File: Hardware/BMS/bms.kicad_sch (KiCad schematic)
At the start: 13 parts, among them J101 Conn_01x02, J102 Conn_02x05_Top_Bottom, J103 Conn_02x02_Counter_Clockwise, U101 74AHC1G08, U103 LTV-356T, U402 TSC2011IST

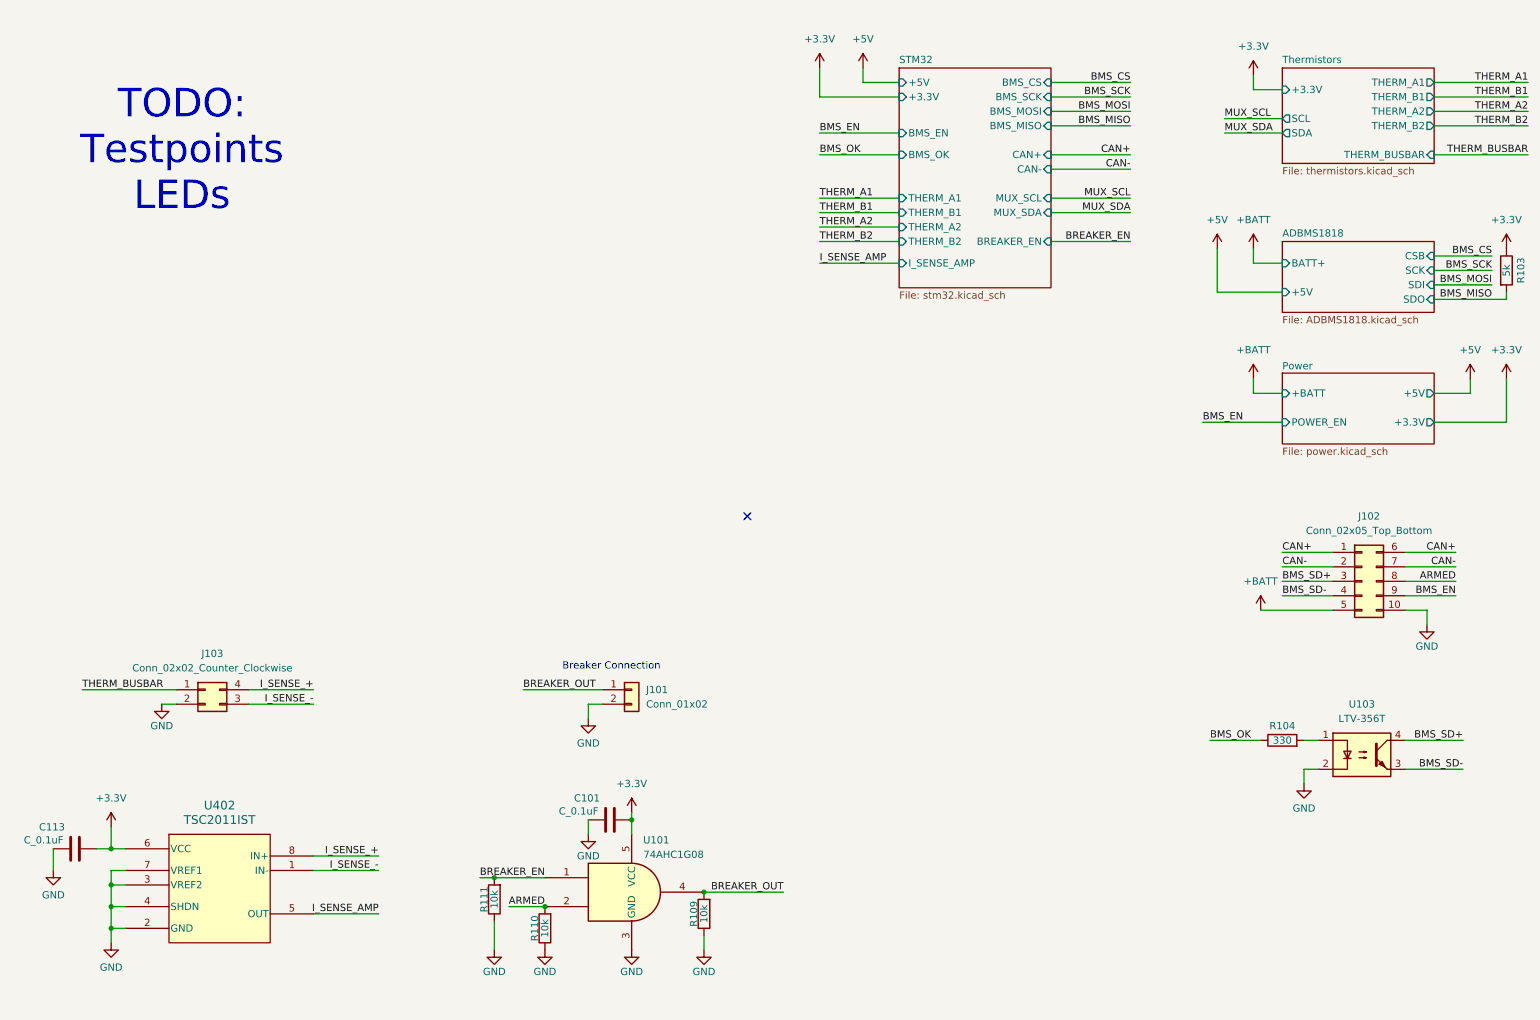
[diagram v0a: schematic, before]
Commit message: Add test points and LEDs
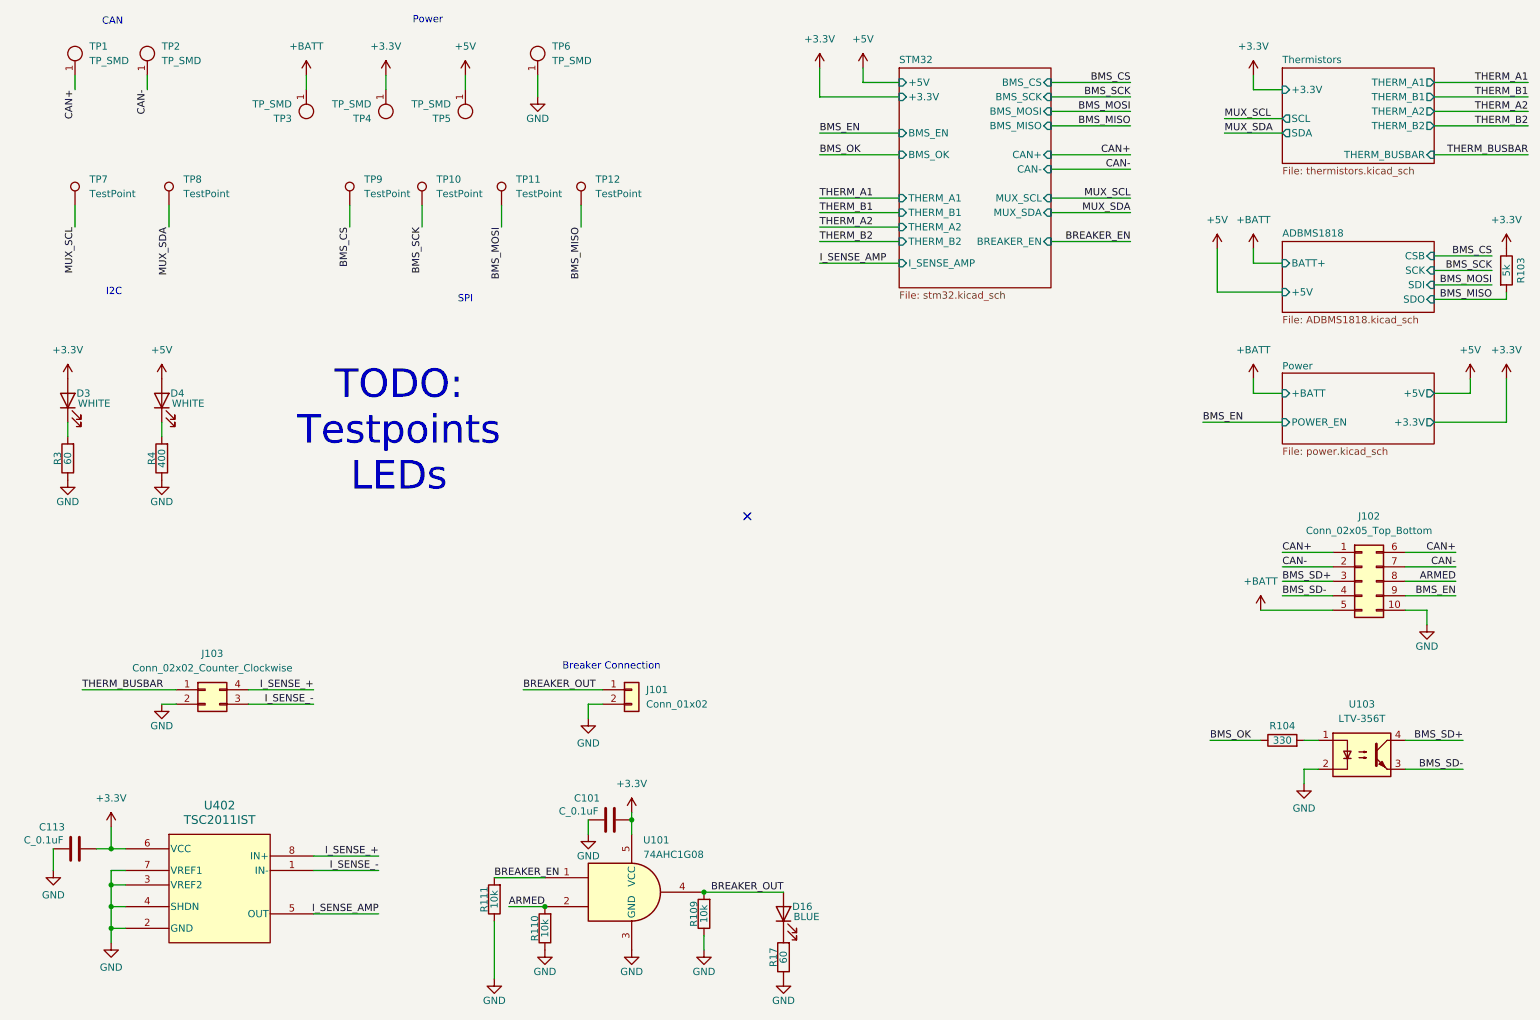
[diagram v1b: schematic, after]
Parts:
- added D16: BLUE, LED_SMD:LED_0805_2012Metric, symbol Device:LED
- added D3, D4: WHITE, LED_SMD:LED_0805_2012Metric, symbol Device:LED
- added R17, R3: 60, Resistor_SMD:R_0603_1608Metric, symbol Device:R
- added R4: 400, Resistor_SMD:R_0603_1608Metric, symbol Device:R
- added TP1, TP2, TP3, TP4, TP5, TP6: TP_SMD, TestPoint:TestPoint_Keystone_5019_Miniature, symbol formula:TP_SMD
- added TP10, TP11, TP12, TP7, TP8, TP9: TestPoint, TestPoint:TestPoint_Pad_1.0x1.0mm, symbol Connector:TestPoint
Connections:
- net +3.3V: now also D3.2 (A), TP4.1
- net +5V: now also D4.2 (A), TP5.1
- net +BATT: now also TP3.1
- net BMS_CS: now also TP9.1
- net BMS_MISO: now also TP12.1
- net BMS_MOSI: now also TP11.1
- net BMS_SCK: now also TP10.1
- net BREAKER_OUT: now also D16.2 (A)
- net CAN+: now also TP1.1
- net CAN-: now also TP2.1
- net GND: now also R17.1, R3.1, R4.1, TP6.1
- net MUX_SCL: now also TP7.1
- net MUX_SDA: now also TP8.1
- new net: D16.1 (K), R17.2
- new net: D4.1 (K), R4.2
- new net: D3.1 (K), R3.2
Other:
- note added: "CAN"
- note added: "I2C"
- note added: "Power"
- note added: "SPI"

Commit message: begin layout
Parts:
- renumbered C113 to C101, C101 to C102, D3 to D101, D4 to D102, D16 to D103, J103 to J101, J101 to J102, J102 to J103, R3 to R101, R4 to R102, R111 to R103, R110 to R104, R109 to R105, R17 to R106, R104 to R107, R103 to R108, TP1 to TP101, TP7 to TP102, TP2 to TP103, TP8 to TP104, TP3 to TP105, TP9 to TP106, TP4 to TP107, TP10 to TP108, TP5 to TP109, TP11 to TP110, TP6 to TP111, TP12 to TP112, U402 to U101, U101 to U102
